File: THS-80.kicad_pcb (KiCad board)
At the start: 4 copper layers, 111.5 x 102.9 mm, 115 parts, among them J1 USB_B_Micro, J10 RC80 Bus, J2 RC80 Bus, J3 IDE, J4 JTAG, J5 PMOD, J6 CTC Header, J7 Port B, J8 Port A, J9 PIO Header, Q1 IRLML6402, Q2 IRLML6402, SW1 Reset, SW2 SW_DIP_x06, U1 DS1813R-5+T&R, U2 MAX40200AUK, U3 CPU -Z84C0020AEG, U4 SRAM - IS62C5128BL-45TLI, U5 SST39SF040, U6 EPM7064STC100, U7 CTC - Z84C3010AEG, U8 SIO/3 - Z84C4310AEG, U9 Z84C2010AEG, X1 CFPS-72 50mhz

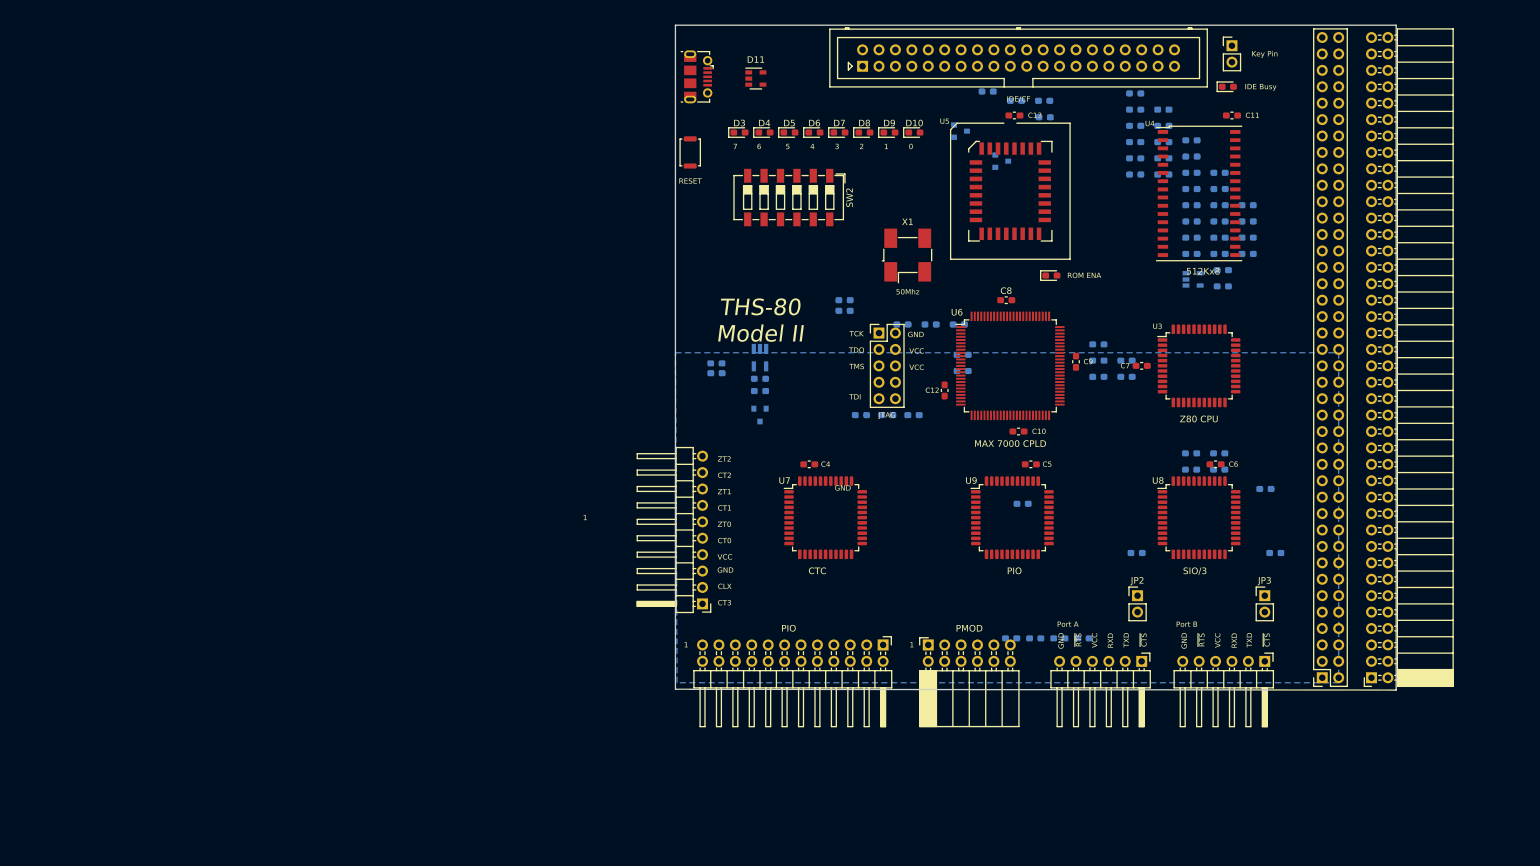
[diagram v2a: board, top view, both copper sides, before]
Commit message: fixed bus connections
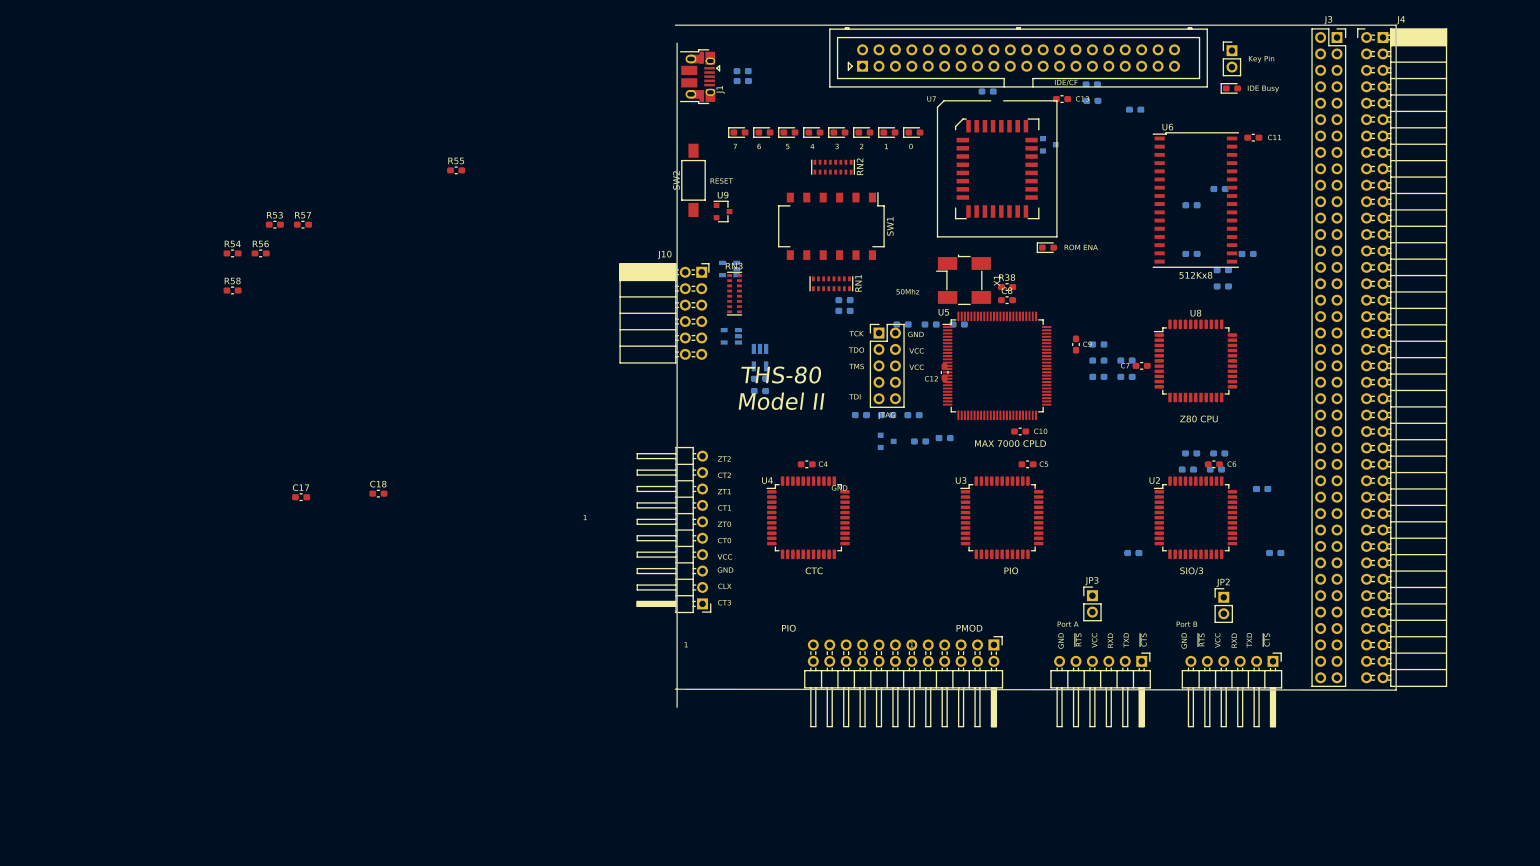
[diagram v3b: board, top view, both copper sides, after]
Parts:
- removed the D11 at (114.3, 39.4)
- removed the J2 at (209.6, 132.1)
- removed the J5 at (141.0, 127.0)
- removed the J9 at (134.0, 127.0)
- removed the R10 at (155.6, 105.2)
- removed the R18 at (181.7, 56.5)
- removed the R19 at (173.0, 54.2)
- removed the R2 at (153.8, 126.0)
- removed the R20 at (177.3, 54.2)
- removed the R21 at (173.0, 51.7)
- removed the R22 at (177.3, 51.7)
- removed the R23 at (173.0, 49.2)
- removed the R24 at (173.0, 46.7)
- removed the R25 at (190.4, 64.0)
- removed the R26 at (177.3, 49.2)
- removed the R27 at (181.7, 54.0)
- removed the R28 at (186.0, 59.0)
- removed the R29 at (190.4, 61.5)
- removed the R3 at (165.0, 126.0)
- removed R32, R33, R34, R35: 200R, Resistor_SMD:R_0603_1608Metric_Pad1.05x0.95mm_HandSolder
- removed the R4 at (161.2, 126.0)
- removed the R5 at (157.5, 126.0)
- removed R52: 10K, Resistor_SMD:R_0603_1608Metric_Pad1.05x0.95mm_HandSolder
- removed the U1 at (114.9, 91.4)
- removed the U3 at (182.9, 83.8)
- removed the U4 at (182.9, 57.1)
- removed the U5 at (153.7, 56.8)
- added D12: SP0504BAHT, Package_TO_SOT_SMD:SOT-23-5, B.Cu at (110.5, 79.2)
- added J3: RC80 Bus, Connector_PinSocket_2.54mm:PinSocket_2x40_P2.54mm_Vertical, F.Cu at (204.2, 33.0)
- added J4: RC80 Expansion, Connector_PinSocket_2.54mm:PinSocket_2x40_P2.54mm_Horizontal, F.Cu at (211.3, 33.0)
- added J6: PIO Header, Connector_PinHeader_2.54mm:PinHeader_2x12_P2.54mm_Horizontal, F.Cu at (151.1, 127.0)
- added R58: 10K, Resistor_SMD:R_0603_1608Metric_Pad1.05x0.95mm_HandSolder, F.Cu at (33.3, 72.2)
- added RN1: 10K, Resistor_SMD:R_Cat16-8, F.Cu at (126.0, 71.1)
- added RN2: 680R, Resistor_SMD:R_Cat16-8, F.Cu at (126.2, 53.1)
- added RN3: 200R, Resistor_SMD:R_Cat16-8, F.Cu at (111.0, 72.6)
- added U6: SRAM - IS62C5128BL-45TLI, Package_SO:TSOP-II-32_21.0x10.2mm_P1.27mm, F.Cu at (182.4, 58.2)
- added U7: SST39SF040, Package_LCC:PLCC-32_SMD-Socket, F.Cu at (151.6, 53.3)
- added U8: CPU -Z84C0020AEG, Package_QFP:LQFP-44_10x10mm_P0.8mm, F.Cu at (182.4, 83.1)
- added U9: DS1813R-5+T&R, Package_TO_SOT_SMD:SOT-23, F.Cu at (109.2, 59.9)
- C17, C18, R53, R54, R55, R56, R57: moved to F.Cu
- J1: footprint Connector_USB:USB_Micro-B_Molex-105017-0001 -> Connector_USB:USB_Micro-B_Amphenol_10103594-0001LF_Horizontal
- J10: value RC80 Bus -> PMOD; footprint Connector_PinSocket_2.54mm:PinSocket_2x40_P2.54mm_Vertical -> Connector_PinSocket_2.54mm:PinSocket_2x06_P2.54mm_Horizontal
- R38: renamed from R11; moved to F.Cu
- SW1: value Reset -> SW_DIP_x06; footprint Button_Switch_SMD:SW_Push_SPST_NO_Alps_SKRK -> Button_Switch_SMD:SW_DIP_SPSTx06_Slide_Omron_A6S-610x_W8.9mm_P2.54mm
- SW2: value SW_DIP_x06 -> Reset; footprint Button_Switch_SMD:SW_DIP_SPSTx06_Slide_6.7x16.8mm_W6.73mm_P2.54mm_LowProfile_JPin -> Button_Switch_SMD:SW_SPST_FSMSM
- U1: renamed from U2; value MAX40200AUK -> MAX40203AUK
- moved R54 157.2 mm to (33.3, 66.4)
- moved R56 144.1 mm to (37.7, 66.4)
- moved C17 143.5 mm to (43.9, 104.1)
- moved R53 142.4 mm to (39.9, 62.0)
- moved R57 141.8 mm to (44.2, 62.0)
- moved C18 135.3 mm to (55.9, 103.6)
- moved R55 118.4 mm to (67.9, 53.6)
- moved J10 114.7 mm to (105.9, 69.3), turned to 0 degrees
- moved D13 71.7 mm to (110.2, 68.8), turned to 180 degrees
- moved Q1 49.3 mm to (134.6, 95.5)
- moved C3 45.4 mm to (112.3, 39.8)
- moved R1 45.4 mm to (112.3, 38.2)
- moved R38 28.9 mm to (153.2, 71.6)
- moved SW1 24.7 mm to (126.0, 62.2)
- moved SW2 15.0 mm to (104.6, 55.1), turned to 90 degrees
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- renumbered C2 to C1, C15 to C14, C14 to C15, C3 to C2, C1 to C3, D9 to D10, D10 to D11, D12 to D2, D2 to D3, D3 to D4, D4 to D5, D5 to D6, D6 to D7, D7 to D8, D8 to D9, J3 to J2, J8 to J5, J6 to J8, J4 to J9, JP3 to JP2, JP2 to JP3, Q2 to Q1, Q1 to Q2, R47 to R10, R51 to R11, R48 to R12, R40 to R13, R41 to R14, R42 to R15, R43 to R16, R50 to R17, R36 to R18, R37 to R19, R6 to R2, R38 to R20, R39 to R21, R12 to R22, R13 to R23, R15 to R24, R16 to R25, R30 to R26, R31 to R27, R14 to R28, R17 to R29, R8 to R3, R9 to R4, R7 to R5, R49 to R6, R44 to R7, R45 to R8, R46 to R9, U8 to U2, U9 to U3, U7 to U4, U6 to U5
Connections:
- D13 pad 1: Net-(D13-Pad1) -> /CPLD/R7
- D13 pad 3: Net-(D13-Pad3) -> /CPLD/R6
- D13 pad 4: Net-(D13-Pad4) -> /CPLD/R5
- D13 pad 5: Net-(D13-Pad5) -> /CPLD/R4
- J10 pad 1: /A15 -> /CPLD/R0
- J10 pad 10: (no net) -> /CPLD/R7
- J10 pad 11: /A10 -> GND
- J10 pad 12: (no net) -> VCC
- J10 pad 2: (no net) -> /CPLD/R1
- J10 pad 3: /A14 -> /CPLD/R2
- J10 pad 4: (no net) -> /CPLD/R3
- J10 pad 5: /A13 -> GND
- J10 pad 6: (no net) -> VCC
- J10 pad 7: /A12 -> /CPLD/R4
- J10 pad 8: (no net) -> /CPLD/R5
- J10 pad 9: /A11 -> /CPLD/R6
- J2 pad 15: /D1 -> /A1
- J2 pad 17: /D0 -> /A0
- R53 pad 2: /CPLD/SW1 -> Net-(R53-Pad2)
- R54 pad 2: /CPLD/SW2 -> /CPU, RAM and ROM/~INT
- R55 pad 2: /CPLD/SW3 -> /CPU, RAM and ROM/~NMI
- R56 pad 2: /CPLD/SW4 -> /CPU, RAM and ROM/~WAIT
- R57 pad 2: /CPLD/SW5 -> (no net)
- SW1 pad 1: /~RESET -> GND
- SW2 pad 1: GND -> /~RESET
- U2 pad 20: /Peripherals/A0 -> /A0
- U2 pad 21: /Peripherals/A1 -> /A1
- U2 pad 24: /Peripherals/D6 -> /D6
- U2 pad 25: /Peripherals/D4 -> /D4
- U2 pad 26: /Peripherals/D2 -> /D2
- U2 pad 27: /Peripherals/A0 -> /A0
- U2 pad 29: /Peripherals/A1 -> /A1
- U2 pad 30: /Peripherals/D3 -> /D3
- U2 pad 31: /Peripherals/D5 -> /D5
- U2 pad 32: /Peripherals/D7 -> /D7
- U2 pad 34: /Peripherals/IEI -> Net-(R58-Pad2)
- U2 pad 35: /Peripherals/IEO -> /Peripherals/CTC_IEI
- U2 pad 5: /CLK_CPU -> /CLK
- U3 pad 11: /Peripherals/A1 -> /A1
- U3 pad 12: /Peripherals/A0 -> /A0
- U3 pad 26: /Peripherals/A0 -> /A0
- U3 pad 27: /Peripherals/A1 -> /A1
- U3 pad 30: /Peripherals/IEO -> (no net)
- U3 pad 31: /Peripherals/IEI -> /Peripherals/PIO_IEI
- U3 pad 33: /CLK_CPU -> /CLK
- U3 pad 4: /Peripherals/D5 -> /D5
- U3 pad 5: /Peripherals/D4 -> /D4
- U3 pad 6: /Peripherals/D3 -> /D3
- U3 pad 7: /Peripherals/D2 -> /D2
- U3 pad 8: /Peripherals/D7 -> /D7
- U3 pad 9: /Peripherals/D6 -> /D6
- U4 pad 1: /Peripherals/A0 -> /A0
- U4 pad 10: /Peripherals/D6 -> /D6
- U4 pad 12: /Peripherals/D7 -> /D7
- U4 pad 2: /Peripherals/A1 -> /A1
- U4 pad 22: /Peripherals/IEO -> /Peripherals/PIO_IEI
- U4 pad 25: /Peripherals/IEI -> /Peripherals/CTC_IEI
- U4 pad 29: /CLK_CPU -> /CLK
- U4 pad 3: /Peripherals/D2 -> /D2
- U4 pad 33: /Peripherals/A0 -> /A0
- U4 pad 35: /Peripherals/A1 -> /A1
- U4 pad 4: /Peripherals/D3 -> /D3
- U4 pad 8: /Peripherals/D4 -> /D4
- U4 pad 9: /Peripherals/D5 -> /D5
- U5 pad 10: /CPLD/A3 -> /CPLD/LED5
- U5 pad 100: (no net) -> /CPLD/LED1
- U5 pad 12: /CPLD/A2 -> /CPLD/LED6
- U5 pad 13: /CPLD/A1 -> /CPLD/LED7
- U5 pad 14: /CPLD/A0 -> /CPLD/SW5
- U5 pad 16: /CPLD/SW5 -> /CPLD/SW4
- U5 pad 17: /CPLD/SW4 -> /CPLD/SW3
- U5 pad 19: /CPLD/SW3 -> /CPLD/SW2
- U5 pad 20: /CPLD/SW2 -> /CPLD/SW1
- U5 pad 21: /CPLD/SW1 -> /CPLD/SW0
- U5 pad 23: /CPLD/SW0 -> /CTC_~CE
- U5 pad 25: (no net) -> /PIO_~CE
- U5 pad 29: (no net) -> /CPLD/PMOD7
- U5 pad 30: (no net) -> /CPLD/PMOD6
- U5 pad 31: /~INT -> /CPLD/PMOD5
- U5 pad 32: /~M1 -> /CPLD/PMOD4
- U5 pad 33: /~MREQ -> /CPLD/PMOD3
- U5 pad 35: /~IORQ -> /CPLD/PMOD2
- U5 pad 36: /~WR -> /CPLD/PMOD1
- U5 pad 37: /~RD -> /CPLD/PMOD0
- U5 pad 40: /RAM_~CE~ -> /~IORQ
- U5 pad 41: /ROM_~CE~ -> /~MREQ
- U5 pad 42: /SIO_~CE -> /~M1
- U5 pad 44: /PIO_~CE -> /SIO_~CE
- U5 pad 45: /CTC_~CE -> (no net)
- U5 pad 46: /IDE_~CE~ -> (no net)
- U5 pad 47: /~PAGE -> /CLK_U
- U5 pad 48: /CLK_CPU -> (no net)
- U5 pad 52: /CLK_U -> /A7
- U5 pad 54: (no net) -> /A6
- U5 pad 56: (no net) -> /A5
- U5 pad 57: (no net) -> /A4
- U5 pad 58: (no net) -> /A3
- U5 pad 6: /CPLD/A6 -> /CPLD/LED2
- U5 pad 60: (no net) -> /A2
- U5 pad 61: /CPLD/PMOD0 -> /A1
- U5 pad 63: /CPLD/PMOD1 -> /A0
- U5 pad 64: /CPLD/PMOD2 -> /A0
- U5 pad 65: /CPLD/PMOD3 -> /A1
- U5 pad 67: /CPLD/PMOD4 -> /D2
- U5 pad 68: /CPLD/PMOD5 -> /D3
- U5 pad 69: /CPLD/PMOD6 -> /D4
- U5 pad 71: /CPLD/PMOD7 -> /D5
- U5 pad 75: /CPLD/LED0 -> /D6
- U5 pad 76: /CPLD/LED1 -> /D7
- U5 pad 79: /CPLD/LED2 -> /~RD
- U5 pad 8: /CPLD/A5 -> /CPLD/LED3
- U5 pad 80: /CPLD/LED3 -> /~WR
- U5 pad 81: /CPLD/LED4 -> (no net)
- U5 pad 83: /CPLD/LED5 -> (no net)
- U5 pad 84: /CPLD/LED6 -> /~PAGE
- U5 pad 85: /CPLD/LED7 -> /IDE_~CE~
- U5 pad 9: /CPLD/A4 -> /CPLD/LED4
- U5 pad 92: /CPLD/A6 -> (no net)
- U5 pad 93: /CPLD/A5 -> (no net)
- U5 pad 94: /CPLD/A4 -> (no net)
- U5 pad 96: /CPLD/A3 -> (no net)
- U5 pad 97: /CPLD/A2 -> (no net)
- U5 pad 98: /CPLD/A1 -> /~INT
- U5 pad 99: /CPLD/A0 -> /CPLD/LED0
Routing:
- removed copper zone on B.Cu, net GND
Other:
- board size 111.5 x 102.9 mm -> 111.5 x 105.5 mm

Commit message: passed DRC
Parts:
- removed the C14 at (194.7, 112.8)
- removed the C4 at (122.2, 99.1)
- removed the C5 at (156.3, 99.1)
- removed the J3 at (204.2, 33.0)
- removed the J6 at (151.1, 127.0)
- removed R54, R55, R56, R57, R58: 10K, Resistor_SMD:R_0603_1608Metric_Pad1.05x0.95mm_HandSolder
- removed the SW2 at (104.6, 55.1)
- removed the U3 at (152.4, 107.3)
- removed the U6 at (182.4, 58.2)
- added C16: 100nF, Capacitor_SMD:C_0603_1608Metric_Pad1.05x0.95mm_HandSolder, F.Cu at (167.6, 83.2)
- added C17: 100nF, Capacitor_SMD:C_0603_1608Metric_Pad1.05x0.95mm_HandSolder, F.Cu at (185.4, 45.1)
- added C18: 100nF, Capacitor_SMD:C_0603_1608Metric_Pad1.05x0.95mm_HandSolder, F.Cu at (151.8, 42.5)
- added C19: 100nF, Capacitor_SMD:C_0603_1608Metric_Pad1.05x0.95mm_HandSolder, F.Cu at (120.0, 101.6)
- added C20: 100nF, Capacitor_SMD:C_0603_1608Metric_Pad1.05x0.95mm_HandSolder, F.Cu at (156.2, 101.6)
- added C21: 100nF, Capacitor_SMD:C_0603_1608Metric_Pad1.05x0.95mm_HandSolder, F.Cu at (177.2, 101.6)
- added J2: RC80 Bus, Connector_PinSocket_2.54mm:PinSocket_2x40_P2.54mm_Vertical, F.Cu at (193.0, 33.0)
- added J7: PIO Header, Connector_PinHeader_2.54mm:PinHeader_2x12_P2.54mm_Horizontal, F.Cu at (141.6, 127.0)
- added R17: 10K, Resistor_SMD:R_0603_1608Metric_Pad1.05x0.95mm_HandSolder, F.Cu at (80.1, 73.6)
- added R18: 10K, Resistor_SMD:R_0603_1608Metric_Pad1.05x0.95mm_HandSolder, F.Cu at (84.4, 71.1)
- added R2: 10K, Resistor_SMD:R_0603_1608Metric_Pad1.05x0.95mm_HandSolder, F.Cu at (80.6, 99.8)
- added R22: 10K, Resistor_SMD:R_0603_1608Metric_Pad1.05x0.95mm_HandSolder, F.Cu at (31.4, 85.5)
- added R3: 10K, Resistor_SMD:R_0603_1608Metric_Pad1.05x0.95mm_HandSolder, F.Cu at (72.1, 104.8)
- added R4: 10K, Resistor_SMD:R_0603_1608Metric_Pad1.05x0.95mm_HandSolder, F.Cu at (80.6, 102.3)
- added R5: 10K, Resistor_SMD:R_0603_1608Metric_Pad1.05x0.95mm_HandSolder, F.Cu at (76.4, 104.8)
- added SW1: Reset, Button_Switch_SMD:SW_SPST_FSMSM, F.Cu at (104.5, 55.1)
- added U5: IS62C5128BL-45TLI, Package_SO:TSOP-II-32_21.0x10.2mm_P1.27mm, F.Cu at (176.4, 54.6)
- added U7: Z84C2010AEG, Package_QFP:LQFP-44_10x10mm_P0.8mm, F.Cu at (151.0, 109.2)
- U2: value SIO/3 - Z84C4310AEG -> DS1813R-5+T&R; footprint Package_QFP:LQFP-44_10x10mm_P0.8mm -> Package_TO_SOT_SMD:SOT-23
- U4: value CTC - Z84C3010AEG -> Z84C0010AEG
- U8: value CPU -Z84C0020AEG -> Z84C4310AEG
- U9: value DS1813R-5+T&R -> Z84C3010AEG; footprint Package_TO_SOT_SMD:SOT-23 -> Package_QFP:LQFP-44_10x10mm_P0.8mm
- moved U2 114.7 mm to (67.7, 105.9)
- moved U4 59.2 mm to (176.4, 83.1)
- moved U9 51.6 mm to (124.5, 109.2)
- moved C6 48.4 mm to (141.0, 79.4), turned to 270 degrees
- moved C11 43.0 mm to (161.3, 79.4), turned to 90 degrees
- moved C7 33.0 mm to (141.0, 83.8), turned to 90 degrees
- moved C13 32.6 mm to (148.6, 72.4), turned to 180 degrees
- moved U8 26.8 mm to (176.4, 109.2)
- moved C8 19.9 mm to (147.3, 92.7), turned to 180 degrees
- moved C9 16.3 mm to (153.0, 92.7), turned to 0 degrees
- moved C12 15.7 mm to (153.0, 72.4), turned to 180 degrees
- moved JP3 11.4 mm to (175.3, 119.4)
- moved J8 11.4 mm to (162.6, 129.5)
- moved J9 11.4 mm to (182.9, 129.5)
- moved JP2 11.4 mm to (154.9, 119.4)
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- renumbered C3 to C1, C17 to C14, C18 to C15, C1 to C2, C2 to C3, C15 to C4, C16 to C5, D13 to D12, D2 to D13, D3 to D2, D12 to D3, J8 to J10, J4 to J3, J2 to J4, J9 to J5, J10 to J6, J7 to J8, J5 to J9, JP3 to JP2, JP2 to JP3, Q2 to Q1, Q1 to Q2, R22 to R10, R23 to R11, R24 to R12, R25 to R13, R28 to R14, R29 to R15, R38 to R16, R26 to R19, R27 to R20, R53 to R21, R13 to R23, R14 to R24, R15 to R25, R16 to R26, R7 to R27, R8 to R28, R9 to R29, R10 to R30, R12 to R31, R6 to R32, R17 to R33, R11 to R34, R18 to R35, R19 to R36, R20 to R37, R21 to R38, R2 to R6, R5 to R7, R3 to R8, R4 to R9, SW1 to SW2, U5 to U3, U7 to U6
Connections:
- J10 pad 3: /Peripherals/ZT0 -> /Peripherals/CLK_A
- J10 pad 5: /Peripherals/ZT1 -> /Peripherals/CLK_B
- J10 pad 7: /Peripherals/ZT2 -> /Peripherals/CLK_C
- J3 pad 44: /~BUSACK -> /~BUSAK
- J3 pad 48: /~BUSREQ -> /~BUSRQ
- J3 pad 53: /A0 -> /D0
- J3 pad 55: /A1 -> /D1
- J4 pad 15: /A1 -> /D1
- J4 pad 17: /A0 -> /D0
- U2 pad 1: (no net) -> /~RESET
- U2 pad 2: /Peripherals/~RTSA -> VCC
- U2 pad 3: /Peripherals/~CTSA -> GND
- U3 pad 1: Net-(U5-Pad1) -> (no net)
- U3 pad 2: Net-(U5-Pad1) -> (no net)
- U3 pad 22: Net-(U5-Pad1) -> (no net)
- U3 pad 24: Net-(U5-Pad1) -> (no net)
- U3 pad 27: Net-(U5-Pad1) -> (no net)
- U3 pad 28: Net-(U5-Pad1) -> (no net)
- U3 pad 48: (no net) -> /CLK_CPU
- U3 pad 49: Net-(U5-Pad1) -> (no net)
- U3 pad 5: Net-(U5-Pad1) -> (no net)
- U3 pad 50: Net-(U5-Pad1) -> (no net)
- U3 pad 53: Net-(U5-Pad1) -> (no net)
- U3 pad 55: Net-(U5-Pad1) -> (no net)
- U3 pad 64: /A0 -> /D0
- U3 pad 65: /A1 -> /D1
- U3 pad 7: Net-(U5-Pad1) -> (no net)
- U3 pad 70: Net-(U5-Pad1) -> (no net)
- U3 pad 72: Net-(U5-Pad1) -> (no net)
- U3 pad 77: Net-(U5-Pad1) -> (no net)
- U3 pad 78: Net-(U5-Pad1) -> (no net)
- U3 pad 81: (no net) -> /RAM_~CE
- U3 pad 83: (no net) -> /ROM_~CE
- U3 pad 88: (no net) -> Net-(R17-Pad1)
- U3 pad 90: (no net) -> Net-(R18-Pad1)
- U3 pad 92: (no net) -> /A16
- U3 pad 93: (no net) -> /A17
- U3 pad 94: (no net) -> /A18
- U3 pad 98: /~INT -> (no net)
- U4 pad 1: /A0 -> /CLK
- U4 pad 10: /D6 -> /D1
- U4 pad 12: /D7 -> /~INT
- U4 pad 13: GND -> /~NMI
- U4 pad 14: /~RD -> /~HALT
- U4 pad 15: (no net) -> /~MREQ
- U4 pad 16: /Peripherals/ZT0 -> /~IORQ
- U4 pad 18: /Peripherals/ZT1 -> /~RD
- U4 pad 19: /Peripherals/ZT2 -> /~WR
- U4 pad 2: /A1 -> /D4
- U4 pad 20: (no net) -> /~BUSAK
- U4 pad 21: /~IORQ -> /~WAIT
- U4 pad 22: /Peripherals/PIO_IEI -> /~BUSRQ
- U4 pad 23: /~INT -> /~RESET
- U4 pad 24: (no net) -> /~M1
- U4 pad 25: /Peripherals/CTC_IEI -> /~RFSH
- U4 pad 26: (no net) -> GND
- U4 pad 27: /~M1 -> /A0
- U4 pad 28: (no net) -> /A1
- U4 pad 29: /CLK -> /A2
- U4 pad 3: /D2 -> /D3
- U4 pad 30: (no net) -> /A3
- U4 pad 31: /CTC_~CE -> /A4
- U4 pad 32: /~RESET -> /A5
- U4 pad 33: /A0 -> (no net)
- U4 pad 34: (no net) -> /A6
- U4 pad 35: /A1 -> /A7
- U4 pad 36: /CLK_U -> /A8
- U4 pad 37: /CLK_U -> /A9
- U4 pad 38: (no net) -> /A10
- U4 pad 4: /D3 -> /D5
- U4 pad 40: /CLK_U -> /A11
- U4 pad 41: /CLK_U -> /A12
- U4 pad 42: (no net) -> /A13
- U4 pad 43: VCC -> /A14
- U4 pad 44: (no net) -> /A15
- U4 pad 5: (no net) -> /D6
- U4 pad 6: (no net) -> VCC
- U4 pad 7: (no net) -> /D2
- U4 pad 8: /D4 -> /D7
- U4 pad 9: /D5 -> /D0
- U6 pad 13: /A0 -> /D0
- U6 pad 14: /A1 -> /D1
- U6 pad 22: /~RD -> /ROM_~CE
- U8 pad 1: /CLK -> (no net)
- U8 pad 10: /A1 -> (no net)
- U8 pad 11: (no net) -> /Peripherals/TXB
- U8 pad 12: /CPU, RAM and ROM/~INT -> /Peripherals/CLK_B
- U8 pad 13: /CPU, RAM and ROM/~NMI -> /Peripherals/CLK_B
- U8 pad 14: (no net) -> /Peripherals/RXB
- U8 pad 15: /~MREQ -> (no net)
- U8 pad 16: /~IORQ -> (no net)
- U8 pad 18: /~RD -> GND
- U8 pad 19: /~WR -> /~RD
- U8 pad 2: /D4 -> /Peripherals/~RTSA
- U8 pad 20: (no net) -> /A0
- U8 pad 21: /CPU, RAM and ROM/~WAIT -> /A1
- U8 pad 22: (no net) -> /SIO_~CE
- U8 pad 23: /~RESET -> /~IORQ
- U8 pad 24: /~M1 -> /D6
- U8 pad 25: (no net) -> /D4
- U8 pad 26: GND -> /D2
- U8 pad 27: /A0 -> /D0
- U8 pad 28: /A1 -> (no net)
- U8 pad 29: /A2 -> /D1
- U8 pad 3: /D3 -> /Peripherals/~CTSA
- U8 pad 30: /A3 -> /D3
- U8 pad 31: /A4 -> /D5
- U8 pad 32: /A5 -> /D7
- U8 pad 33: (no net) -> /~INT
- U8 pad 34: /A6 -> /IEI
- U8 pad 35: /A7 -> /Peripherals/IEO_0
- U8 pad 36: /A8 -> /~M1
- U8 pad 37: /A9 -> VCC
- U8 pad 38: /A10 -> (no net)
- U8 pad 4: /D5 -> GND
- U8 pad 40: /A11 -> (no net)
- U8 pad 41: /A12 -> /Peripherals/RXA
- U8 pad 42: /A13 -> /Peripherals/CLK_A
- U8 pad 43: /A14 -> /Peripherals/CLK_A
- U8 pad 44: /A15 -> /Peripherals/TXA
- U8 pad 5: /D6 -> /CLK_CPU
- U8 pad 6: VCC -> /~RESET
- U8 pad 7: /D2 -> GND
- U8 pad 8: /D7 -> /Peripherals/~CTSB
- U8 pad 9: /A0 -> /Peripherals/~RTSB
- U9 pad 1: /~RESET -> /D0
- U9 pad 2: VCC -> /D1
- U9 pad 3: GND -> /D2
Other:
- board size 111.5 x 105.5 mm -> 101.6 x 101.6 mm
- net class Default: via_dia 0.6858 -> 0.4572; via_drill 0.3302 -> 0.2286
- net class Power added: clearance 0.1524, trace_width 0.4064, via_dia 0.8128, via_drill 0.4064
- rule solder_mask_min_width: 0.254 -> 0.1016
- rule via_min_drill: 0.3302 -> 0.2286
- rule via_min_size: 0.6858 -> 0.4572
- board text added: "THS-80 Model I"
- board text removed: "THS-80 Model II"

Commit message: started routing
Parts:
- added C22: 100uF, Capacitor_SMD:C_1206_3216Metric_Pad1.42x1.75mm_HandSolder, B.Cu at (185.4, 74.9)
- added C23: 100nF, Capacitor_SMD:C_0603_1608Metric_Pad1.05x0.95mm_HandSolder, B.Cu at (188.0, 74.9)
- C14, C15, R17, R18, R2, R21, R3, R4, R5: moved to B.Cu
- C2: value 100nF -> 2.2nF
- C3: value 1uF -> .33uF
- C5, D13: moved to F.Cu
- moved R22 149.7 mm to (180.3, 100.3), turned to 270 degrees
- moved R21 113.0 mm to (152.4, 51.4), turned to 90 degrees
- moved R5 105.8 mm to (180.3, 85.1), turned to 270 degrees
- moved R3 104.4 mm to (174.6, 85.1), turned to 270 degrees
- moved R4 99.4 mm to (178.4, 85.1), turned to 270 degrees
- moved R2 93.3 mm to (172.7, 85.1), turned to 270 degrees
- moved R35 79.9 mm to (109.2, 119.4), turned to 180 degrees
- moved R17 71.8 mm to (151.8, 78.1), turned to 270 degrees
- moved R37 67.7 mm to (109.2, 109.2), turned to 180 degrees
- moved R15 67.4 mm to (121.9, 90.2)
- moved R36 67.2 mm to (109.2, 114.3), turned to 180 degrees
- moved R14 66.8 mm to (121.9, 88.3)
- moved R18 65.8 mm to (149.9, 78.1), turned to 270 degrees
- moved R12 65.8 mm to (121.9, 81.3)
- moved C14 65.0 mm to (106.7, 87.0)
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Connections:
- C3 pad 1: VCC -> Net-(C3-Pad1)
- C4 pad 1: Net-(C4-Pad1) -> VCC
- D12 pad 1: /CPLD/R7 -> /CPLD/R4
- D12 pad 3: /CPLD/R6 -> /CPLD/R5
- D12 pad 4: /CPLD/R5 -> /CPLD/R6
- D12 pad 5: /CPLD/R4 -> /CPLD/R7
- J1 pad 1: Net-(J1-Pad1) -> Net-(C3-Pad1)
- J4 pad 20: Net-(C4-Pad1) -> Net-(J4-Pad20)
- J5 pad 6: VCC -> (no net)
- JP1 pad 1: Net-(C4-Pad1) -> Net-(J4-Pad20)
- RN2 pad 1: Net-(D11-Pad2) -> Net-(D4-Pad2)
- RN2 pad 2: Net-(D10-Pad2) -> Net-(D5-Pad2)
- RN2 pad 3: Net-(D9-Pad2) -> Net-(D6-Pad2)
- RN2 pad 4: Net-(D8-Pad2) -> Net-(D7-Pad2)
- RN2 pad 5: Net-(D7-Pad2) -> Net-(D8-Pad2)
- RN2 pad 6: Net-(D6-Pad2) -> Net-(D9-Pad2)
- RN2 pad 7: Net-(D5-Pad2) -> Net-(D10-Pad2)
- RN2 pad 8: Net-(D4-Pad2) -> Net-(D11-Pad2)
- U1 pad 1: Net-(J1-Pad1) -> Net-(C3-Pad1)
- U1 pad 3: Net-(J1-Pad1) -> Net-(C3-Pad1)
- U3 pad 45: (no net) -> /~WAIT
- U3 pad 92: /A16 -> (no net)
- U3 pad 93: /A17 -> (no net)
- U3 pad 94: /A18 -> (no net)
- U3 pad 96: (no net) -> /A16
- U3 pad 97: (no net) -> /A17
- U3 pad 98: (no net) -> /A18
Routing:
- net /D5: track 0.00 -> 175.8 mm, vias 0 -> 14
- net /D4: track 0.00 -> 169.9 mm, vias 0 -> 12
- net /D3: track 0.00 -> 167.7 mm, vias 0 -> 12
- net /D6: track 0.00 -> 164.5 mm, vias 0 -> 8
- net /D2: track 0.00 -> 162.8 mm, vias 0 -> 13
- net /D0: track 0.00 -> 149.9 mm, vias 0 -> 8
- net /A2: track 0.00 -> 135.6 mm, vias 0 -> 7
- net /D7: track 0.00 -> 133.5 mm, vias 0 -> 9
- net /D1: track 0.00 -> 127.6 mm, vias 0 -> 9
- net /A0: track 0.00 -> 127.4 mm, vias 0 -> 5
- net /A15: track 0.00 -> 111.9 mm, vias 0 -> 7
- net /A1: track 0.00 -> 109.3 mm, vias 0 -> 5
- net /A12: track 0.00 -> 94.1 mm, vias 0 -> 3
- net /A5: track 0.00 -> 91.7 mm, vias 0 -> 3
- net /A4: track 0.00 -> 88.7 mm, vias 0 -> 3
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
